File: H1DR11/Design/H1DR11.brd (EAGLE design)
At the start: 34.6 x 30 mm, 34 parts, among them P1 HEXABIT_17.32_NO_P6, U1 STM32F091CBU6, U2 MAX14840EASAT, X1 XTALL_CSTCE8M00G52

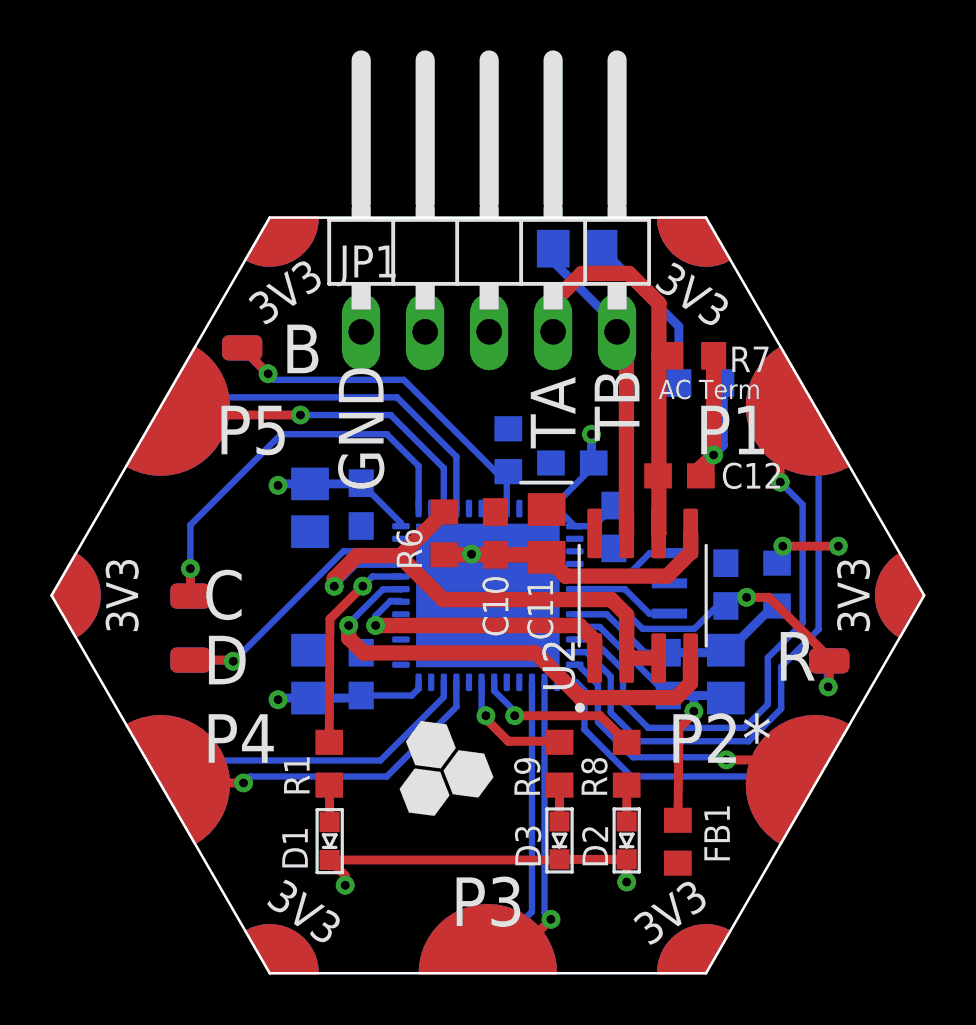
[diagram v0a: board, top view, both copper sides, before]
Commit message: mirror pin header
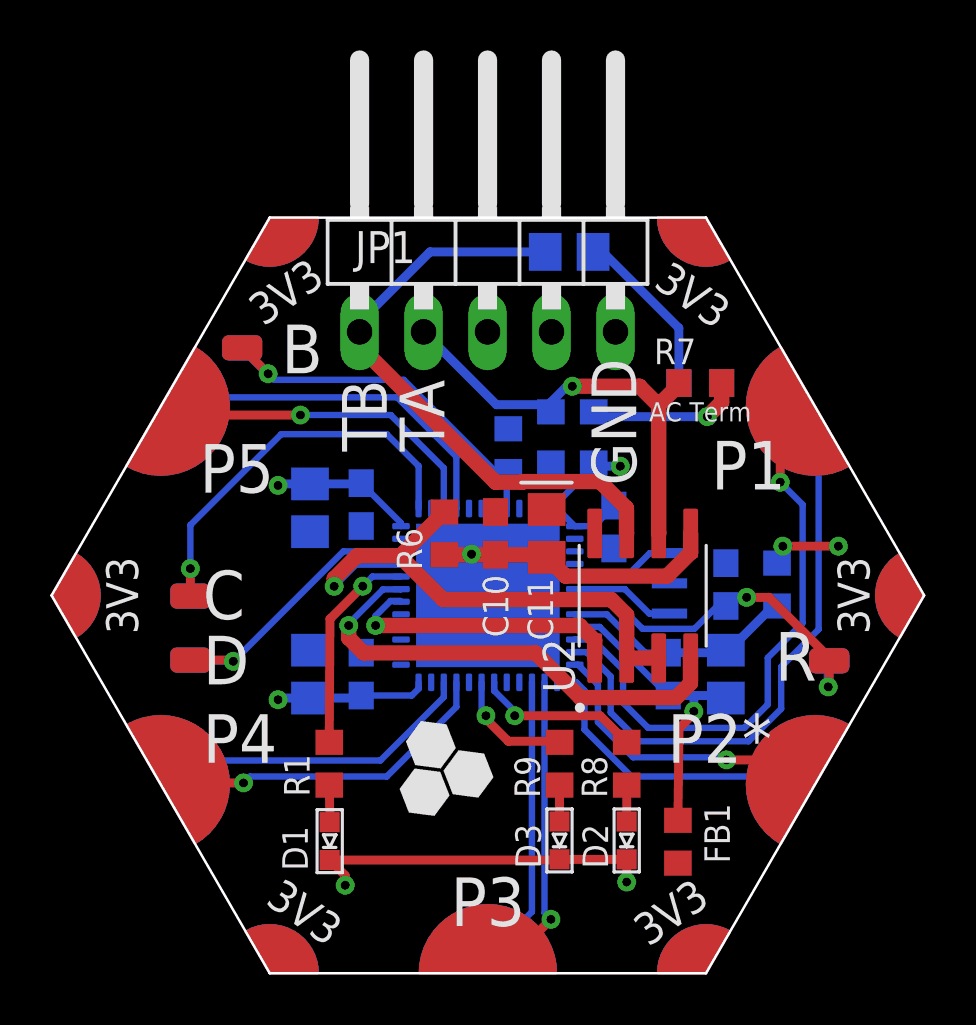
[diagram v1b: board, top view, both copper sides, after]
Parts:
- moved C12 4.96 mm to (38.0, 41.9), flipped to the bottom, turned to 180 degrees
- moved R7 1.13 mm to (43.1, 43.1)
- moved R5 0.34 mm to (37.8, 48.3)
- moved JP1 0.06 mm to (34.6, 48.9)
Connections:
- net GND: now also JP1.5; no longer JP1.1
- net TA: now also JP1.2; no longer JP1.4
- net TB: now also JP1.1; no longer JP1.5
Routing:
- net TB: track 12.5 -> 24.3 mm
- net TA: track 16.5 -> 18.5 mm, vias 0 -> 1

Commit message: 3way terminal block  was added
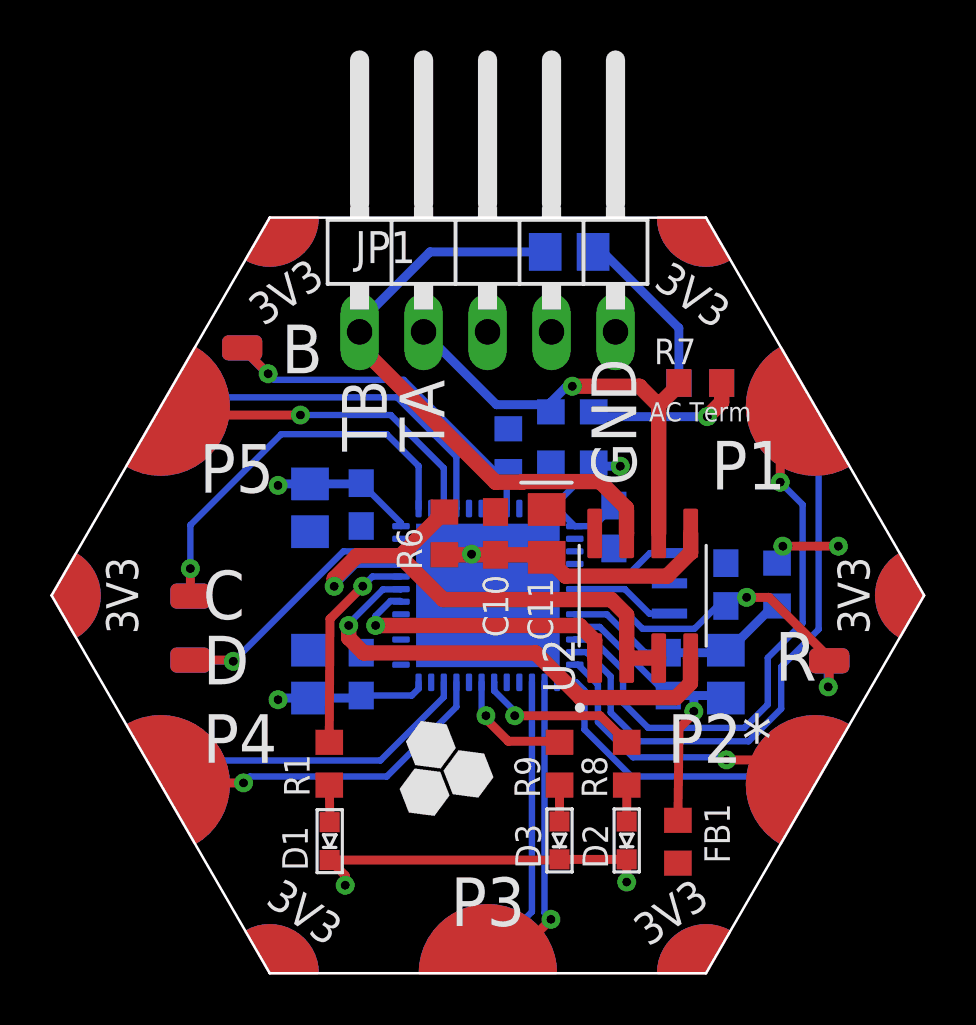
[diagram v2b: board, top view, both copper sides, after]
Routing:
- net TA: track 18.5 -> 17.9 mm
- net TB: track 24.3 -> 23.8 mm
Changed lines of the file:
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@@
 <contactref element="U2" pad="7"/>
 <contactref element="R5" pad="1"/>
-<wire x1="36.8985" y1="48.26" x2="36.8985" y2="47.747" width="0.3556" layer="16"/>
 <contactref element="JP1" pad="1"/>
 <wire x1="29.5275" y1="45.085" x2="29.5275" y2="45.466" width="0.3556" layer="16"/>
@@
 <contactref element="U2" pad="6"/>
 <contactref element="C12" pad="1"/>
-<wire x1="41.402" y1="37.0825" x2="41.40925" y2="37.08975" width="0.6096" layer="1"/>
 <contactref element="R7" pad="2"/>
 <contactref element="JP1" pad="2"/>
-<wire x1="32.0675" y1="44.5525" x2="32.0675" y2="45.085" width="0.3556" layer="1"/>
 <wire x1="42.2147625" y1="42.9895" x2="42.203" y2="43.053" width="0.508" layer="1"/>
 <wire x1="41.402" y1="37.0825" x2="41.402" y2="42.1767375" width="0.6096" layer="1"/>

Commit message: output CAM files generated
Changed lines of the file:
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@@
 <?xml version="1.0" encoding="utf-8"?>
 <!DOCTYPE eagle SYSTEM "eagle.dtd">
-<eagle version="9.6.0">
+<eagle version="9.6.1">
 <drawing>
 <settings>
@@
 </layers>
 <board>
+<fusionsync huburn="a.cGVyc29uYWw6dWUyYWRmNjYx" projecturn="a.cGVyc29uYWw6dWUyYWRmNjYxIzIwMjAwNDI4MjkyMjA3NzAx" f3durn="urn:adsk.wipprod:dm.lineage:0bZKyB_8Qeyj0L_032PeSA" pcbguid="a5c2f18c-d076-412a-8650-0f549dc6bdb3" lastpulledtime="" lastsyncedchangeguid="" latestrevisionid="fd9aabbc-0468-4404-8163-9c2b3434560e" lastsyncedrevisionid="fd9aabbc-0468-4404-8163-9c2b3434560e" lastboardhashguid="c8d83414-8a95-2411-081f-f96d024df18d" lastpushedtime="2020-05-04T08:58:15Z" linktopcb3d="%12"/>
 <plain>
 <text x="27.3867875" y="43.37405625" size="1.9304" layer="26" rot="MR0">B</text>
@@
 </element>
 <element name="JP1" library="Hexabitz" package="1X05/90" package3d_urn="urn:adsk.eagle:package:22467/2" value="" x="34.6075" y="48.895" smashed="yes">
-<attribute name="NAME" x="31.75" y="49.0855" size="1.27" layer="25" ratio="10" rot="R180"/>
+<attribute name="DESCRIPTION" value="Conn Header R/a 5POS 2.54MM MALE" x="34.6075" y="48.895" size="1.778" layer="27" display="off"/>
+<attribute name="MFN" value="Sullins" x="34.6075" y="48.895" size="1.778" layer="27" display="off"/>
+<attribute name="MPN" value="PEC05SBAN" x="34.6075" y="48.895" size="1.778" layer="27" display="off"/>
+<attribute name="NAME" x="31.623" y="48.8315" size="1.016" layer="25" ratio="10" rot="R180"/>
+<attribute name="OCTOPART_URL" value="https://octopart.com/pec05sban-sullins-264498?r=sp" x="34.6075" y="48.895" size="1.778" layer="27" display="off"/>
 <attribute name="POPULARITY" value="9" x="34.6075" y="48.895" size="1.778" layer="27" display="off"/>
 <attribute name="VALUE" x="42.8625" y="45.085" size="1.27" layer="27" rot="R90"/>
@@
 <compatibility>
 <note version="8.3" severity="warning">
+Since Version 8.3, EAGLE supports Fusion synchronisation.
+This feature will not be available in this version and saving
+the document will break the link to the Fusion PCB feature.
+</note>
+<note version="8.3" severity="warning">
 Since Version 8.3, EAGLE supports URNs for individual library
